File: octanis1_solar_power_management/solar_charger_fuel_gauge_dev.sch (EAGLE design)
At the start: 116 parts, among them IC1 REG1117, IC401 TUSB2046BIRHBIRHB, Q2 32.768kHz, Q4 CSTCR4M00G15L99, Q401 CSTCR6M00G15L99, T1 BC547, T2 BC547, U1 BQ24210, U2 BQ27510_DRZ_12, U3 DRV8836DSSR, U4 DRV8836DSSR, U402 TPS62237DRY, U404 TPD2E001DRLR, U5 DRV8836DSSR, U6 MSP430F5529IPNR, U7 DRV8836DSSR

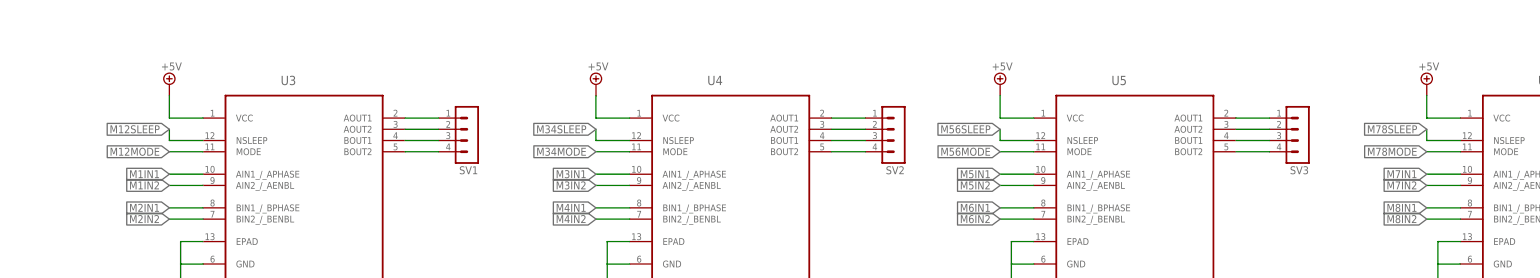
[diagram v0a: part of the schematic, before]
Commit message: connected h-bridges to pins
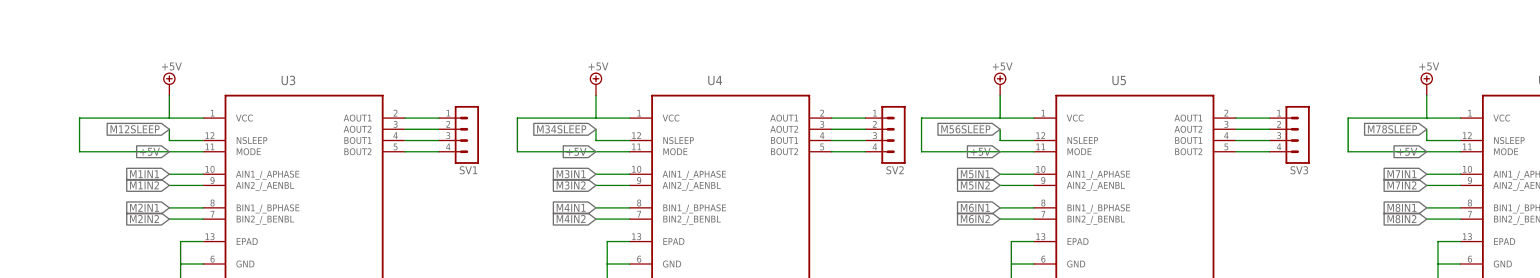
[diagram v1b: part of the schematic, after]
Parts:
- RPUC, RPUD: device resistor:R-EU_R1206 -> rcl:R-EU_R0603
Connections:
- removed net M12MODE: U3.MODE
- removed net M34MODE: U4.MODE
- removed net M56MODE: U5.MODE
- removed net M78MODE: U7.MODE
- net +5V: now also U3.MODE, U4.MODE, U5.MODE, U7.MODE
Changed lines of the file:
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@@
 <part name="R412" library="rcl" deviceset="R-EU_" device="R0402" value="15k"/>
 <part name="GND17" library="supply1" deviceset="GND" device=""/>
-<part name="RPUD" library="resistor" deviceset="R-EU_" device="R1206" value="10k"/>
-<part name="RPUC" library="resistor" deviceset="R-EU_" device="R1206" value="10k"/>
+<part name="RPUD" library="rcl" deviceset="R-EU_" device="R0603" value="10k"/>
+<part name="RPUC" library="rcl" deviceset="R-EU_" device="R0603" value="10k"/>
 <part name="+3V6" library="supply1" deviceset="+3V3" device=""/>
 <part name="GND13" library="supply1" deviceset="GND" device=""/>
@@
 <wire x1="627.38" y1="53.34" x2="627.38" y2="58.42" width="0.1524" layer="91"/>
 <pinref part="SUPPLY6" gate="+5V" pin="+5V"/>
+<pinref part="U3" gate="A" pin="MODE"/>
+<label x="627.38" y="45.72" size="1.778" layer="95" rot="R180" xref="yes"/>
+<wire x1="635" y1="45.72" x2="607.06" y2="45.72" width="0.1524" layer="91"/>
+<wire x1="607.06" y1="45.72" x2="607.06" y2="53.34" width="0.1524" layer="91"/>
+<wire x1="607.06" y1="53.34" x2="627.38" y2="53.34" width="0.1524" layer="91"/>
 </segment>
 <segment>
@@
 <wire x1="723.9" y1="53.34" x2="723.9" y2="58.42" width="0.1524" layer="91"/>
 <pinref part="SUPPLY8" gate="+5V" pin="+5V"/>
+<pinref part="U4" gate="A" pin="MODE"/>
+<label x="723.9" y="45.72" size="1.778" layer="95" rot="R180" xref="yes"/>
+<wire x1="731.52" y1="45.72" x2="706.12" y2="45.72" width="0.1524" layer="91"/>
+<wire x1="706.12" y1="45.72" x2="706.12" y2="53.34" width="0.1524" layer="91"/>
+<wire x1="706.12" y1="53.34" x2="723.9" y2="53.34" width="0.1524" layer="91"/>
 </segment>
 <segment>
@@
 <wire x1="815.34" y1="53.34" x2="815.34" y2="58.42" width="0.1524" layer="91"/>
 <pinref part="SUPPLY9" gate="+5V" pin="+5V"/>
+<pinref part="U5" gate="A" pin="MODE"/>
+<label x="815.34" y="45.72" size="1.778" layer="95" rot="R180" xref="yes"/>
+<wire x1="822.96" y1="45.72" x2="797.56" y2="45.72" width="0.1524" layer="91"/>
+<wire x1="797.56" y1="45.72" x2="797.56" y2="53.34" width="0.1524" layer="91"/>
+<wire x1="797.56" y1="53.34" x2="815.34" y2="53.34" width="0.1524" layer="91"/>
 </segment>
 <segment>
@@
 <wire x1="911.86" y1="53.34" x2="911.86" y2="58.42" width="0.1524" layer="91"/>
 <pinref part="SUPPLY10" gate="+5V" pin="+5V"/>
+<pinref part="U7" gate="A" pin="MODE"/>
+<label x="911.86" y="45.72" size="1.778" layer="95" rot="R180" xref="yes"/>
+<wire x1="919.48" y1="45.72" x2="894.08" y2="45.72" width="0.1524" layer="91"/>
+<wire x1="894.08" y1="45.72" x2="894.08" y2="53.34" width="0.1524" layer="91"/>
+<wire x1="894.08" y1="53.34" x2="911.86" y2="53.34" width="0.1524" layer="91"/>
 </segment>
 </net>
@@
 </segment>
 </net>
-<net name="M12MODE" class="0">
-<segment>
-<pinref part="U3" gate="A" pin="MODE"/>
-<wire x1="635" y1="45.72" x2="627.38" y2="45.72" width="0.1524" layer="91"/>
-<label x="627.38" y="45.72" size="1.778" layer="95" rot="R180" xref="yes"/>
-</segment>
-</net>
 <net name="M1IN1" class="0">
 <segment>
@@
 </segment>
 </net>
-<net name="M34MODE" class="0">
-<segment>
-<pinref part="U4" gate="A" pin="MODE"/>
-<wire x1="731.52" y1="45.72" x2="723.9" y2="45.72" width="0.1524" layer="91"/>
-<label x="723.9" y="45.72" size="1.778" layer="95" rot="R180" xref="yes"/>
-</segment>
-</net>
 <net name="M3IN1" class="0">
 <segment>
@@
 </segment>
 </net>
-<net name="M56MODE" class="0">
-<segment>
-<pinref part="U5" gate="A" pin="MODE"/>
-<wire x1="822.96" y1="45.72" x2="815.34" y2="45.72" width="0.1524" layer="91"/>
-<label x="815.34" y="45.72" size="1.778" layer="95" rot="R180" xref="yes"/>
-</segment>
-</net>
 <net name="M5IN1" class="0">
 <segment>
@@
 </segment>
 </net>
-<net name="M78MODE" class="0">
-<segment>
-<pinref part="U7" gate="A" pin="MODE"/>
-<wire x1="919.48" y1="45.72" x2="911.86" y2="45.72" width="0.1524" layer="91"/>
-<label x="911.86" y="45.72" size="1.778" layer="95" rot="R180" xref="yes"/>
-</segment>
-</net>

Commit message: h-bridge: connected sleep pin with mode pin
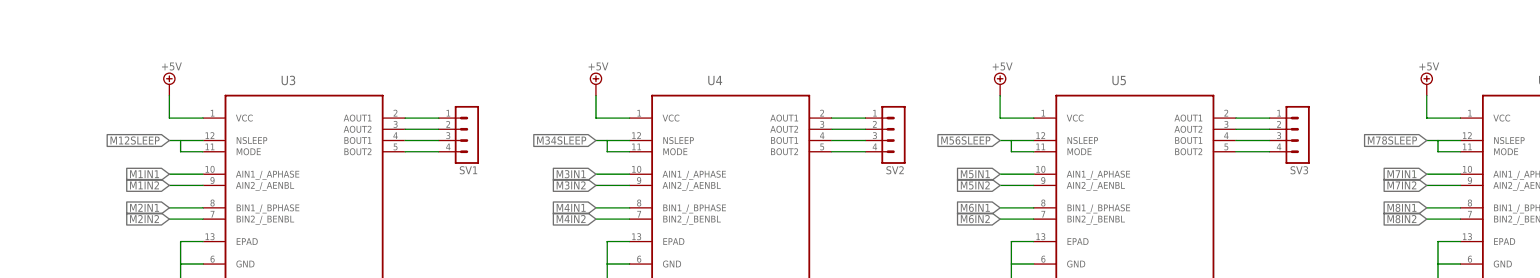
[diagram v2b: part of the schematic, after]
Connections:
- net +5V: no longer U3.MODE, U4.MODE, U5.MODE, U7.MODE
- net M12SLEEP: now also U3.MODE
- net M34SLEEP: now also U4.MODE
- net M56SLEEP: now also U5.MODE
- net M78SLEEP: now also U7.MODE
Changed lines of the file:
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@@
 <wire x1="627.38" y1="53.34" x2="627.38" y2="58.42" width="0.1524" layer="91"/>
 <pinref part="SUPPLY6" gate="+5V" pin="+5V"/>
-<pinref part="U3" gate="A" pin="MODE"/>
-<label x="627.38" y="45.72" size="1.778" layer="95" rot="R180" xref="yes"/>
-<wire x1="635" y1="45.72" x2="607.06" y2="45.72" width="0.1524" layer="91"/>
-<wire x1="607.06" y1="45.72" x2="607.06" y2="53.34" width="0.1524" layer="91"/>
-<wire x1="607.06" y1="53.34" x2="627.38" y2="53.34" width="0.1524" layer="91"/>
-</segment>
-<segment>
+</segment>
+<segment>
+<pinref part="SUPPLY8" gate="+5V" pin="+5V"/>
 <pinref part="U4" gate="A" pin="VCC"/>
 <wire x1="731.52" y1="53.34" x2="723.9" y2="53.34" width="0.1524" layer="91"/>
 <wire x1="723.9" y1="53.34" x2="723.9" y2="58.42" width="0.1524" layer="91"/>
-<pinref part="SUPPLY8" gate="+5V" pin="+5V"/>
-<pinref part="U4" gate="A" pin="MODE"/>
-<label x="723.9" y="45.72" size="1.778" layer="95" rot="R180" xref="yes"/>
-<wire x1="731.52" y1="45.72" x2="706.12" y2="45.72" width="0.1524" layer="91"/>
-<wire x1="706.12" y1="45.72" x2="706.12" y2="53.34" width="0.1524" layer="91"/>
-<wire x1="706.12" y1="53.34" x2="723.9" y2="53.34" width="0.1524" layer="91"/>
 </segment>
 <segment>
@@
 <wire x1="815.34" y1="53.34" x2="815.34" y2="58.42" width="0.1524" layer="91"/>
 <pinref part="SUPPLY9" gate="+5V" pin="+5V"/>
-<pinref part="U5" gate="A" pin="MODE"/>
-<label x="815.34" y="45.72" size="1.778" layer="95" rot="R180" xref="yes"/>
-<wire x1="822.96" y1="45.72" x2="797.56" y2="45.72" width="0.1524" layer="91"/>
-<wire x1="797.56" y1="45.72" x2="797.56" y2="53.34" width="0.1524" layer="91"/>
-<wire x1="797.56" y1="53.34" x2="815.34" y2="53.34" width="0.1524" layer="91"/>
 </segment>
 <segment>
@@
 <wire x1="911.86" y1="53.34" x2="911.86" y2="58.42" width="0.1524" layer="91"/>
 <pinref part="SUPPLY10" gate="+5V" pin="+5V"/>
-<pinref part="U7" gate="A" pin="MODE"/>
-<label x="911.86" y="45.72" size="1.778" layer="95" rot="R180" xref="yes"/>
-<wire x1="919.48" y1="45.72" x2="894.08" y2="45.72" width="0.1524" layer="91"/>
-<wire x1="894.08" y1="45.72" x2="894.08" y2="53.34" width="0.1524" layer="91"/>
-<wire x1="894.08" y1="53.34" x2="911.86" y2="53.34" width="0.1524" layer="91"/>
 </segment>
 </net>
@@
 <segment>
 <pinref part="U3" gate="A" pin="NSLEEP"/>
-<wire x1="635" y1="48.26" x2="627.38" y2="48.26" width="0.1524" layer="91"/>
-<wire x1="627.38" y1="48.26" x2="627.38" y2="50.8" width="0.1524" layer="91"/>
-<label x="627.38" y="50.8" size="1.778" layer="95" rot="R180" xref="yes"/>
+<wire x1="635" y1="48.26" x2="629.92" y2="48.26" width="0.1524" layer="91"/>
+<wire x1="629.92" y1="48.26" x2="627.38" y2="48.26" width="0.1524" layer="91"/>
+<label x="627.38" y="48.26" size="1.778" layer="95" rot="R180" xref="yes"/>
+<pinref part="U3" gate="A" pin="MODE"/>
+<wire x1="635" y1="45.72" x2="629.92" y2="45.72" width="0.1524" layer="91"/>
+<wire x1="629.92" y1="45.72" x2="629.92" y2="48.26" width="0.1524" layer="91"/>
 </segment>
 </net>
@@
 <segment>
 <pinref part="U4" gate="A" pin="NSLEEP"/>
-<wire x1="731.52" y1="48.26" x2="723.9" y2="48.26" width="0.1524" layer="91"/>
-<wire x1="723.9" y1="48.26" x2="723.9" y2="50.8" width="0.1524" layer="91"/>
-<label x="723.9" y="50.8" size="1.778" layer="95" rot="R180" xref="yes"/>
+<wire x1="731.52" y1="48.26" x2="726.44" y2="48.26" width="0.1524" layer="91"/>
+<wire x1="726.44" y1="48.26" x2="723.9" y2="48.26" width="0.1524" layer="91"/>
+<label x="723.9" y="48.26" size="1.778" layer="95" rot="R180" xref="yes"/>
+<pinref part="U4" gate="A" pin="MODE"/>
+<wire x1="731.52" y1="45.72" x2="726.44" y2="45.72" width="0.1524" layer="91"/>
+<wire x1="726.44" y1="45.72" x2="726.44" y2="48.26" width="0.1524" layer="91"/>
 </segment>
 </net>
@@
 <segment>
 <pinref part="U5" gate="A" pin="NSLEEP"/>
-<wire x1="822.96" y1="48.26" x2="815.34" y2="48.26" width="0.1524" layer="91"/>
-<wire x1="815.34" y1="48.26" x2="815.34" y2="50.8" width="0.1524" layer="91"/>
-<label x="815.34" y="50.8" size="1.778" layer="95" rot="R180" xref="yes"/>
+<wire x1="822.96" y1="48.26" x2="817.88" y2="48.26" width="0.1524" layer="91"/>
+<wire x1="817.88" y1="48.26" x2="815.34" y2="48.26" width="0.1524" layer="91"/>
+<label x="815.34" y="48.26" size="1.778" layer="95" rot="R180" xref="yes"/>
+<pinref part="U5" gate="A" pin="MODE"/>
+<wire x1="822.96" y1="45.72" x2="817.88" y2="45.72" width="0.1524" layer="91"/>
+<wire x1="817.88" y1="45.72" x2="817.88" y2="48.26" width="0.1524" layer="91"/>
 </segment>
 </net>
@@
 <segment>
 <pinref part="U7" gate="A" pin="NSLEEP"/>
-<wire x1="919.48" y1="48.26" x2="911.86" y2="48.26" width="0.1524" layer="91"/>
-<wire x1="911.86" y1="48.26" x2="911.86" y2="50.8" width="0.1524" layer="91"/>
-<label x="911.86" y="50.8" size="1.778" layer="95" rot="R180" xref="yes"/>
-</segment>
-</net>
+<wire x1="919.48" y1="48.26" x2="914.4" y2="48.26" width="0.1524" layer="91"/>
+<wire x1="914.4" y1="48.26" x2="911.86" y2="48.26" width="0.1524" layer="91"/>
+<label x="911.86" y="48.26" size="1.778" layer="95" rot="R180" xref="yes"/>
+<pinref part="U7" gate="A" pin="MODE"/>
+<wire x1="919.48" y1="45.72" x2="914.4" y2="45.72" width="0.1524" layer="91"/>
+<wire x1="914.4" y1="45.72" x2="914.4" y2="48.26" width="0.1524" layer="91"/>
+</segment>
+</net>

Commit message: deleted unnecessary components from launchpad board. rearranged
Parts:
- removed C15, C16: 220n, rcl:C-EUC0402
- removed C17: 1n, rcl:C-EUC0402
- removed C23, C24: 10p, rcl:C-EUC0402
- removed C27, C403: 4u7, rcl:CPOL-EUA/3216-18R
- removed C401, C404: 1u, CAP:CSMD0805
- removed C402, C407, C408: 100n, rcl:C-EUC0402
- removed C405, C406, C409, C410, C411, C412: 22p, rcl:C-EUC0402
- removed IC401: TUSB2046BIRHBIRHB, texas:TUSB2046BIRHBIRHB
- removed J401: (no value), usb_con-update:USB_MICRO_FLIPPED
- removed L401: 2.2uH (NR3010T2R2M), MSP-EXP430F5659:L-NR3010
- removed Q2: 32.768kHz, microcrystal:MS3V-T1R
- removed Q4: CSTCR4M00G15L99, murata:MURATA-FILTER_CSTCR6M00G53Z
- removed Q401: CSTCR6M00G15L99, murata:MURATA-FILTER_CSTCR6M00G53Z
- removed R14: 100R, rcl:R-EU_R0402
- removed R15: 1k4, rcl:R-EU_R0402
- removed R27, R404: 47k, rcl:R-EU_R0402
- removed R31, R32: 27R, rcl:R-EU_R0402
- removed R401: 33R, rcl:R-EU_R0402
- removed R402: 10k, rcl:R-EU_R0402
- removed R403, R407: 1k5, rcl:R-EU_R0402
- removed R405, R406, R410, R411, R416, R417: 22R, rcl:R-EU_R0402
- removed R408, R409, R412, R413, R414, R415, R418, R419: 15k, rcl:R-EU_R0402
- removed S3: RST, electricalmeter:PB
- removed S5: BSL, electricalmeter:PB
- removed U402: TPS62237DRY, tps62231dry:TPS6223X_DRY_6
- removed U404: TPD2E001DRLR, Project7264:TPD2E001
- added JP1: SBW, pinhead:PINHD-1X2
- added Q1: 32.768kHz, crystal:FC-12M
- C14, C18, C19, C25, C26, C29: device rcl:C-EUC0402 -> rcl:C-EUC0603
- R16, R28: device rcl:R-EU_R0402 -> rcl:R-EU_R0603
- SOLAR: value (none) -> SOLAR
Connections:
- net SOLAR+ renamed VCC
- removed net !OC: IC401G$1.!OVRCUR1, IC401G$1.!OVRCUR2, IC401G$1.!OVRCUR3, IC401G$1.!OVRCUR4, R402.2
- removed net !PWRON: IC401G$1.!PWRON1, IC401G$1.!PWRON2, IC401G$1.!PWRON3, IC401G$1.!PWRON4
- removed net EZFET_VBUS: C402.1, C403.+, C404.2, J401.VBUS, U402.EN, U402.VIN, U404.VCC
- removed net EZFET_VCC: C401.2, C407.1, IC401G$1.!EXTMEM, IC401G$1.BUSPWR, IC401G$1.EEDATA/GANGED, IC401G$1.VCC, IC401G$1.VCC@1, L401.2, R402.1, R403.1, R404.1, U402.FB
- removed net HUB_DM1: R31.1, R416.2, R419.1
- removed net HUB_DM2: R410.2, R415.1
- removed net HUB_DP1: R32.1, R417.2, R418.1
- removed net HUB_DP2: R411.2, R414.1
- removed net N$14: R14.1, S5.S
- removed net N$15: J401.SHIELD1, R401.1
- removed net N$16: J401.D+, R405.2, U404.IO2
- removed net N$17: J401.D-, R406.2, U404.IO1
- removed net N$18: C406.1, IC401G$1.DM0, R406.1
- removed net N$19: C405.1, IC401G$1.DP0, R403.2, R405.1
- removed net N$20: C412.1, IC401G$1.DM1, R416.1
- removed net N$21: C411.1, IC401G$1.DP1, R417.1
- removed net N$22: C409.1, IC401G$1.DP2, R411.1
- removed net N$23: C410.1, IC401G$1.DM2, R410.1
- removed net N$24: L401.1, U402.SW
- removed net N$25: IC401G$1.XTAL2, R407.2
- removed net N$26: C408.1, IC401G$1.!RESET, R404.2
- removed net N$27: IC401G$1.DP4, R408.2
- removed net N$28: IC401G$1.DM4, R409.2
- removed net N$29: IC401G$1.DP3, R412.2
- removed net N$30: IC401G$1.DM3, R413.2
- removed net N$31: Q401.3, R407.1
- removed net N$32: IC401G$1.XTAL1, Q401.1
- removed net P4.7: U6.54
- removed net P5.2/XT2IN: Q4.3, U6.69
- removed net P5.3/XT2OUT: Q4.1, U6.70
- removed net P7.4: U6.57
- removed net P8.1: U6.16
- removed net P8.2: U6.17
- removed net TARGET_DM: C24.1, R31.2, U6.64
- removed net TARGET_VUSB: C16.1, U6.66
- removed net V18: C15.1, U6.67
- net +3V3: no longer R27.2, S5.P
- net +5V: no longer C27.+, U6.65
- net GND: no longer C15.2, C16.2, C17.2, C23.2, C24.2, C27.-, C401.1, C402.2, C403.-, C404.1, C405.2, C406.2, C407.2, C408.2, C409.2, C410.2, C411.2, C412.2, IC401G$1.GND, IC401G$1.GND@1, IC401G$1.TSTMODE, IC401G$1.TSTPLL/48MCLK, J401.GND, Q2.GND, Q4.2, Q401.2, R401.2, R408.1, R409.1, R412.1, R413.1, R414.2, R415.2, R418.2, R419.2, S3.P, U402.GND, U402.MODE, U404.GND
- net P5.4/XIN: now also Q1.2; no longer Q2.2
- net P5.5/XOUT: now also Q1.1; no longer Q2.1
- net RST/SBWTDIO: now also JP1.1; no longer C17.1, R27.1, S3.S
- net TARGET_DP: no longer C23.1, R15.2, R32.2
- net TARGET_PUR: no longer R14.2, R15.1
- net TEST/SBWTCK: now also JP1.2
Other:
- note removed: "BSL"
- note removed: "RESET"
- note removed: "Speed"
- note removed: "USB Hub and Power"
- note removed: "XT2"
- moved on the sheet: R16, SOLAR, SV1, SV2, SV3, SV4, U3, U4, U5, U7
